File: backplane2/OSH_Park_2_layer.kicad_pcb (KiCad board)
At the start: 2 copper layers, 27 parts, among them J1 Conn_02x40_Odd_Even, J10 Conn_01x40, J11 Conn_01x40, J12 Conn_01x40, J13 Conn_01x40, J14 Conn_01x40, J15 Conn_01x40, J16 Conn_01x40, J17 Conn_01x40, J18 Conn_01x40, J19 Conn_01x40, J2 Conn_02x40_Odd_Even, J20 Conn_01x02, J21 OSTTA020161, J3 Conn_02x40_Odd_Even, J4 Conn_02x40_Odd_Even, J5 Conn_02x40_Odd_Even, J6 Conn_02x40_Odd_Even, J7 Conn_02x40_Odd_Even

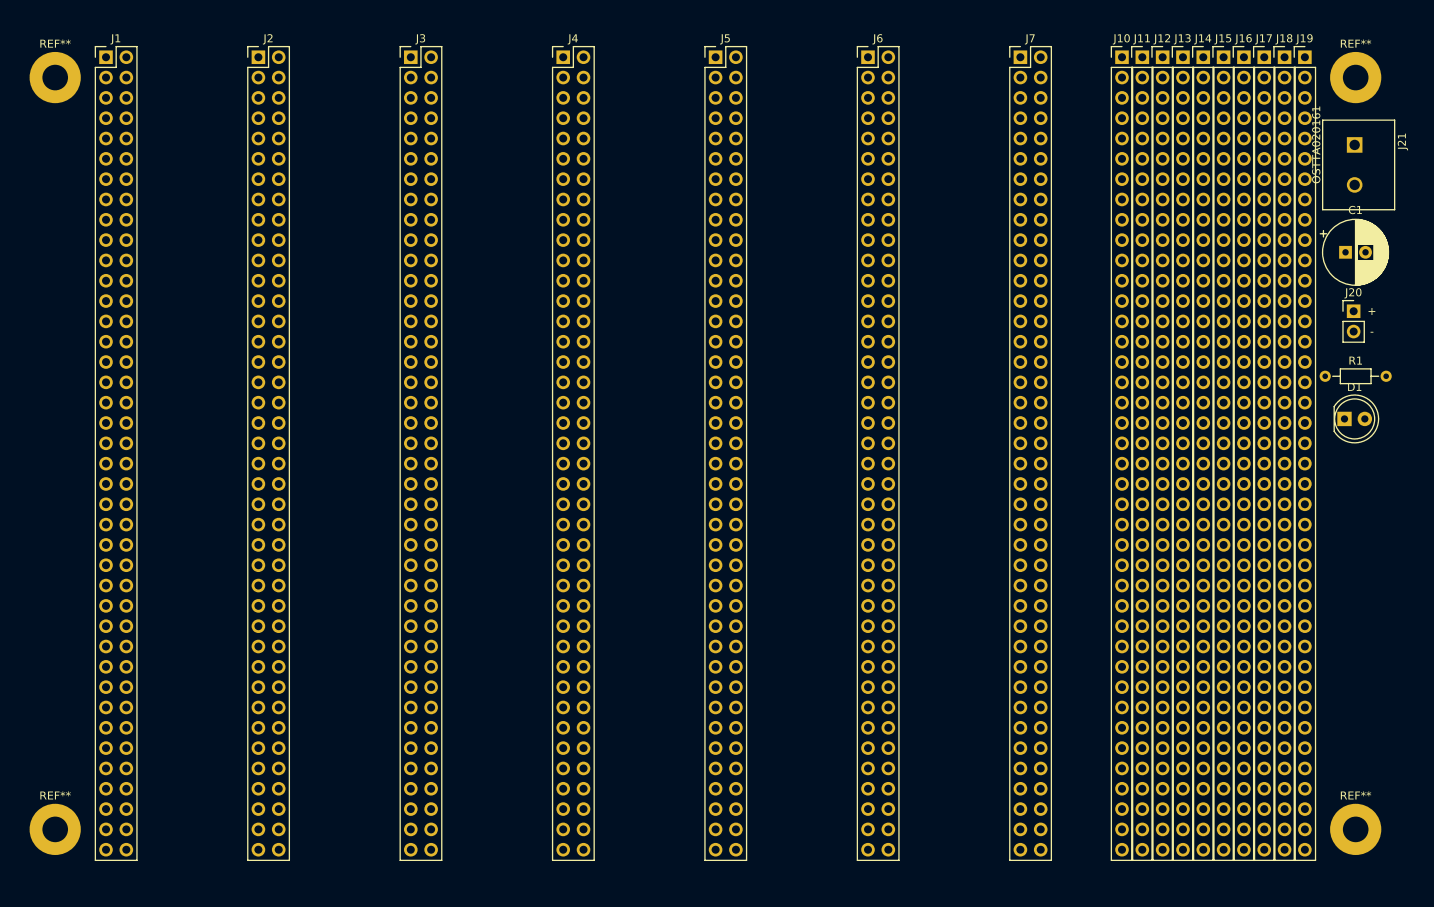
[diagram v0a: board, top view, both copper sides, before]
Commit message: routed half of the backplane connections
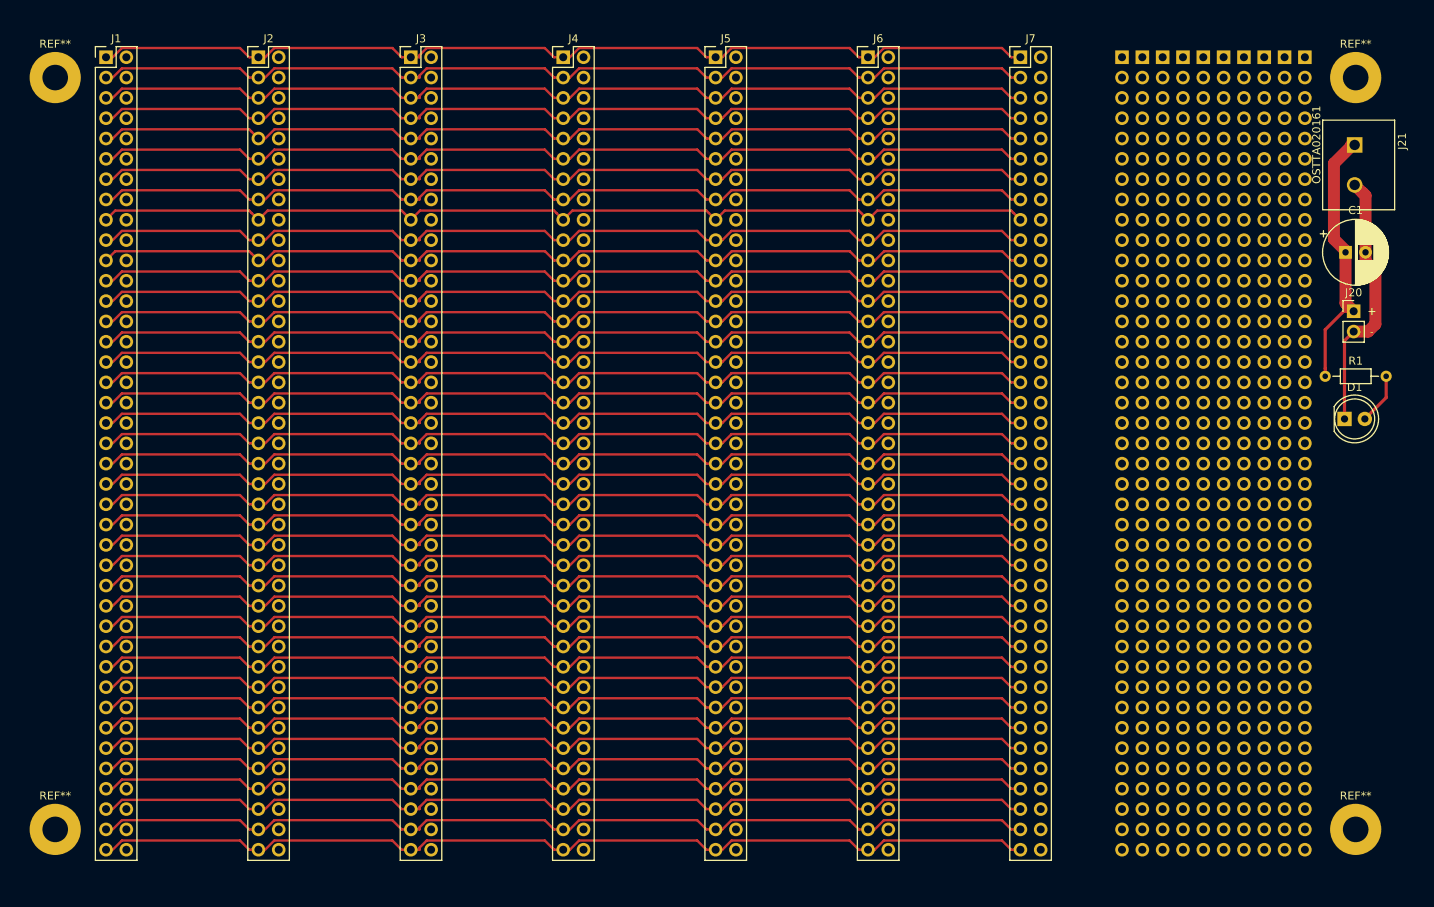
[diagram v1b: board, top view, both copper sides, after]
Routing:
- net /D1: track 0.00 -> 120.3 mm
- net /D17: track 0.00 -> 120.0 mm
- net /D9: track 0.00 -> 119.3 mm
- net /D21: track 0.00 -> 119.3 mm
- net /D79: track 0.00 -> 118.5 mm
- net /D65: track 0.00 -> 118.5 mm
- net /D49: track 0.00 -> 118.5 mm
- net /D45: track 0.00 -> 118.5 mm
- net /D31: track 0.00 -> 118.5 mm
- net /D13: track 0.00 -> 118.5 mm
- net /D7: track 0.00 -> 118.5 mm
- net /D5: track 0.00 -> 118.5 mm
- net /D3: track 0.00 -> 118.5 mm
- net /D11: track 0.00 -> 118.5 mm
- net /D77: track 0.00 -> 118.5 mm
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
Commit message: completely routed?
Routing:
- net /D80: track 0.00 -> 120.0 mm
- net /D66: track 0.00 -> 120.0 mm
- net /D50: track 0.00 -> 120.0 mm
- net /D46: track 0.00 -> 120.0 mm
- net /D32: track 0.00 -> 120.0 mm
- net /D14: track 0.00 -> 120.0 mm
- net /D8: track 0.00 -> 120.0 mm
- net /D6: track 0.00 -> 120.0 mm
- net /D4: track 0.00 -> 120.0 mm
- net /D10: track 0.00 -> 120.0 mm
- net /D36: track 0.00 -> 120.0 mm
- net /D18: track 0.00 -> 120.0 mm
- net /D2: track 0.00 -> 120.0 mm
- net /D78: track 0.00 -> 120.0 mm
- net /D76: track 0.00 -> 120.0 mm
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- added copper zone on B.Cu, net GND
- added copper zone on F.Cu, net VCC
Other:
- board outline added: 174.2 x 109.2 mm
- board text added: "generic passive backplane https://github.com/daveho/easycpu/backplane2 v0.1 30-Oct-2019"

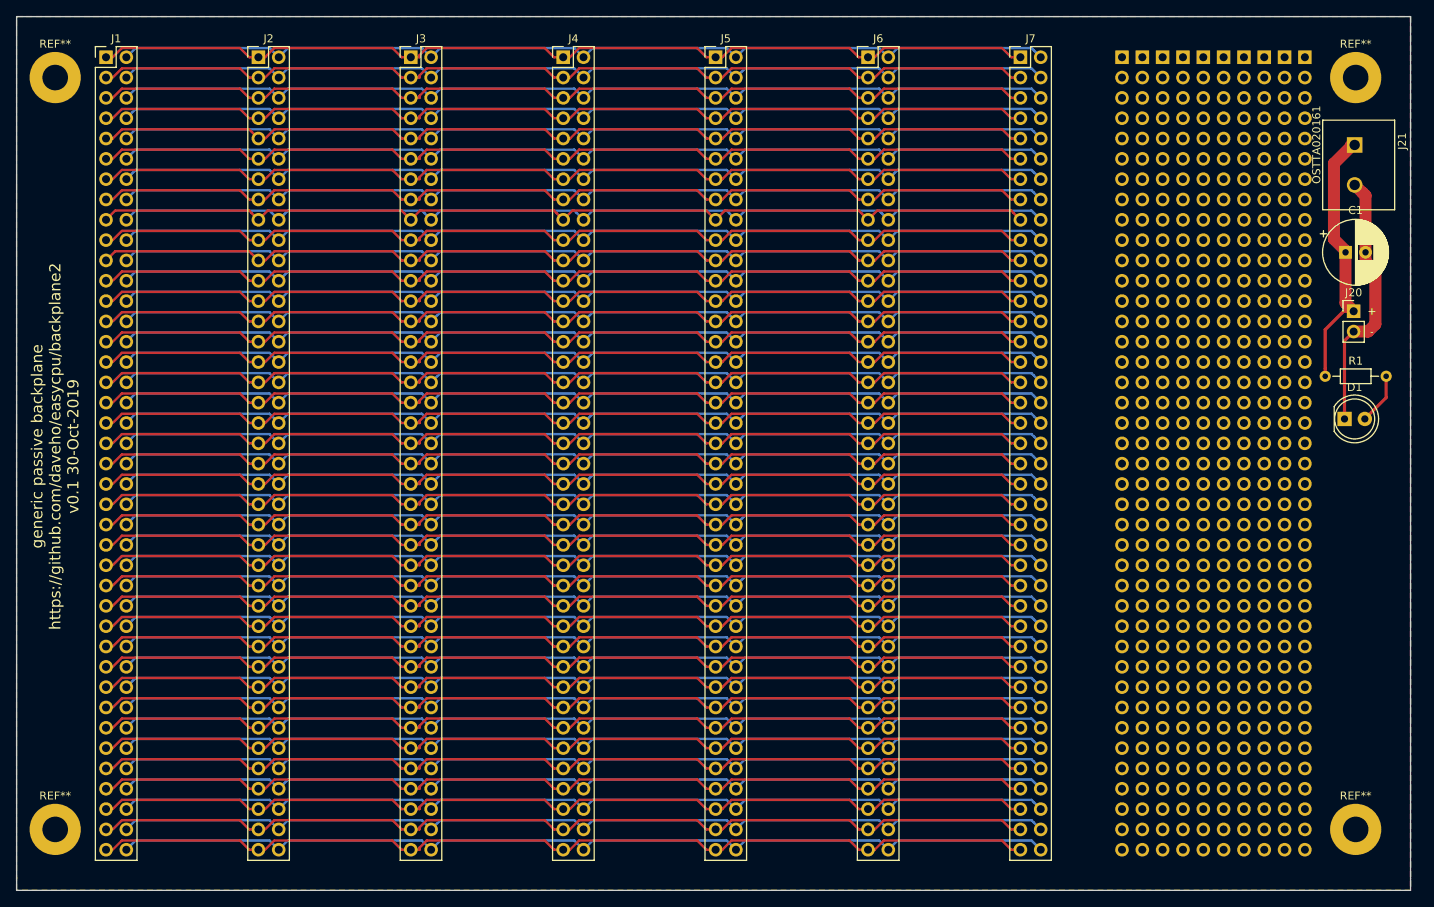
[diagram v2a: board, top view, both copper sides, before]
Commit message: added 4 power distribution traces
also fixed a couple of unconnected nets
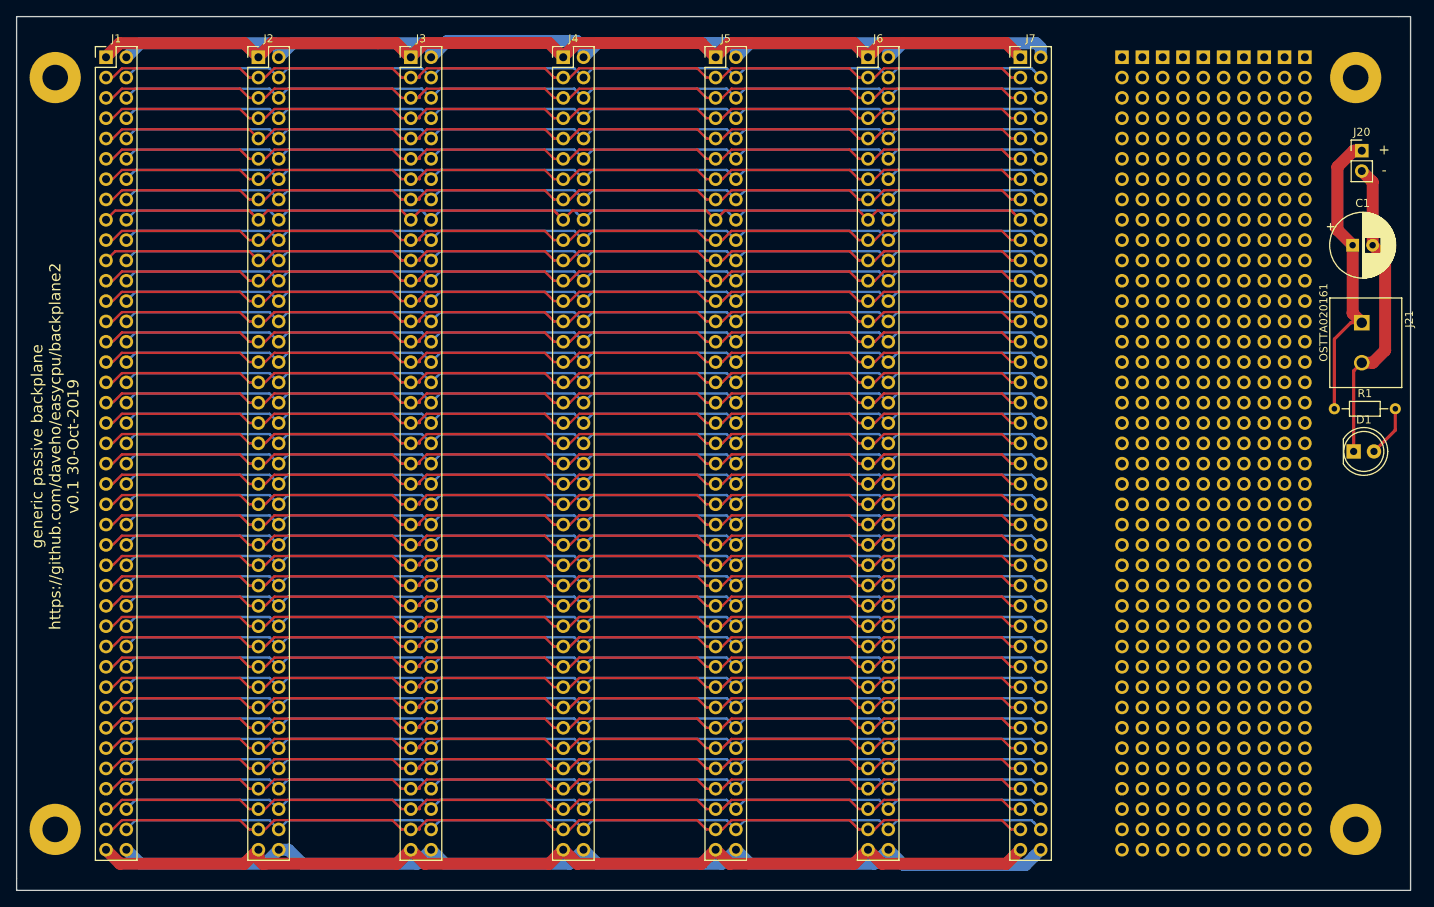
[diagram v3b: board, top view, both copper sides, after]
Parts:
- moved J21 22.2 mm to (207.8, 86.5)
- moved J20 20.1 mm to (207.8, 62.5)
- moved R1 4.22 mm to (204.3, 94.7)
- moved D1 4.22 mm to (206.8, 100.1)
- moved C1 1.26 mm to (206.6, 74.3)
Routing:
- net /D2: track 120.0 -> 127.5 mm
- net /D79: track 118.5 -> 124.5 mm
- net GND: track 33.0 -> 38.7 mm
- net /D1: track 120.3 -> 124.3 mm
- net /D80: track 120.0 -> 123.1 mm
- net VCC: track 34.5 -> 37.6 mm
- net /D21: track 119.3 -> 120.2 mm
- net /D9: track 119.3 -> 120.2 mm
- removed copper zone on B.Cu, net GND
- removed copper zone on F.Cu, net VCC

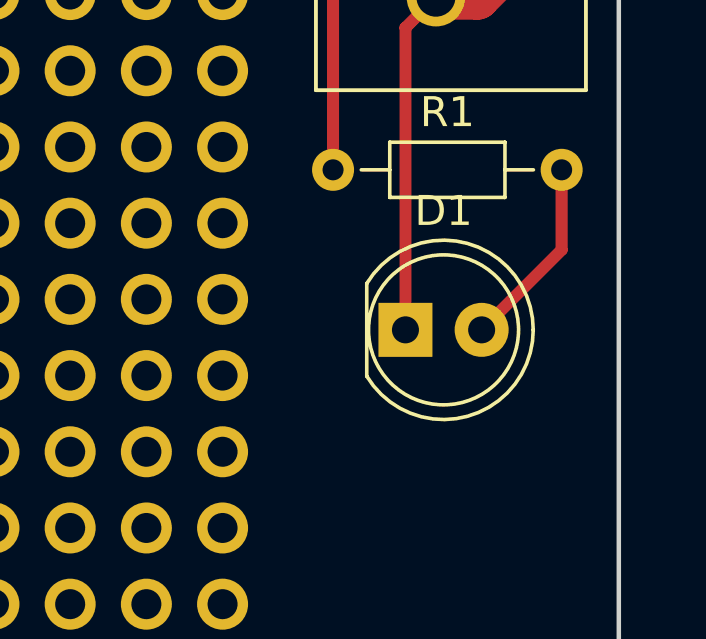
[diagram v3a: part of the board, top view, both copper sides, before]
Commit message: minor tweak to power LED placement
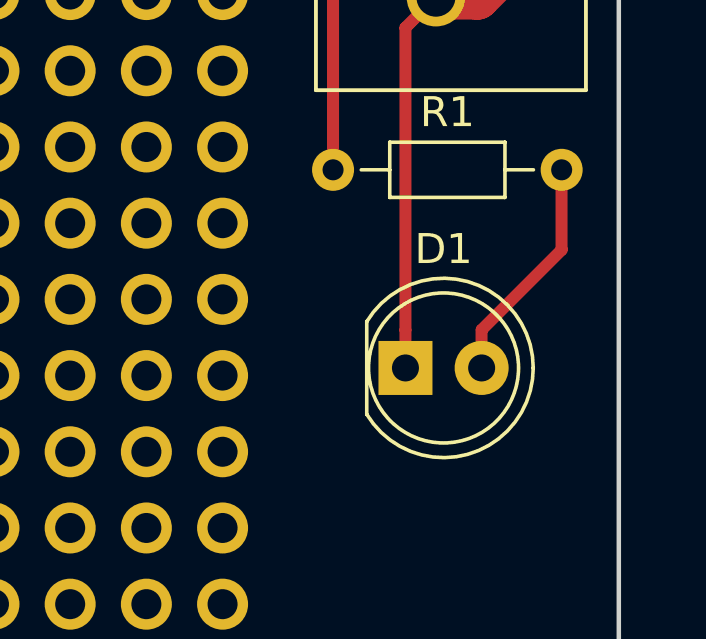
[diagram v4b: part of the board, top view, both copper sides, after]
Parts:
- moved D1 1.27 mm to (206.8, 101.3)
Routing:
- net Net-(D1-Pad2): track 6.44 -> 7.71 mm
- net GND: track 38.7 -> 40.0 mm
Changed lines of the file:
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@@
     (thickness 1.6)
     (drawings 10)
-    (tracks 2126)
+    (tracks 2128)
     (zones 0)
     (modules 27)
@@
   )
   (setup
-    (last_trace_width 0.3)
+    (last_trace_width 0.4)
     (user_trace_width 0.1524)
     (user_trace_width 0.2)
@@
   )
   (module LED_THT:LED_D5.0mm (layer F.Cu)
-    (at 206.756 100.076)
+    (at 206.756 101.346)
     (descr "LED, diameter 5.0mm, 2 pins, http://cdn-reichelt.de/documents/datenblatt/A500/LL-504BC2E-009.pdf")
     (tags "LED diameter 5.0mm 2 pins")
@@
   (segment (start 206.756 90.003) (end 207.772 88.987) (width 0.4) (layer F.Cu) (net 2))
   (segment (start 206.756 100.076) (end 206.756 90.003) (width 0.4) (layer F.Cu) (net 2))
+  (segment (start 206.756 100.076) (end 206.756 101.346) (width 0.4) (layer F.Cu) (net 2))
   (segment (start 211.963 97.409) (end 211.963 94.742) (width 0.4) (layer F.Cu) (net 3))
   (segment (start 209.296 100.076) (end 211.963 97.409) (width 0.4) (layer F.Cu) (net 3))
+  (segment (start 209.296 100.076) (end 209.296 101.346) (width 0.4) (layer F.Cu) (net 3))
   (segment (start 70.637599 151.612401) (end 72.39 149.86) (width 1.5) (layer B.Cu) (net 4))
   (segment (start 53.34 149.86) (end 55.092401 151.612401) (width 1.5) (layer B.Cu) (net 4))

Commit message: updated date (ready to fab now?)
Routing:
- added copper zone on B.Cu, net GND
- added copper zone on F.Cu, net VCC
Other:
- board text added: "generic passive backplane https://github.com/daveho/easycpu/backplane2 v0.1 31-Oct-2019"
- board text removed: "generic passive backplane https://github.com/daveho/easycpu/backplane2 v0.1 30-Oct-2019"
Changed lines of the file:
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@@
   (gr_line (start 212.344 45.72) (end 213.868 45.72) (layer Edge.Cuts) (width 0.15))
   (gr_line (start 39.624 45.72) (end 212.344 45.72) (layer Edge.Cuts) (width 0.15))
-  (gr_text "generic passive backplane\nhttps://github.com/daveho/easycpu/backplane2\nv0.1 30-Oct-2019" (at 44.45 99.441 90) (layer F.SilkS)
+  (gr_text "generic passive backplane\nhttps://github.com/daveho/easycpu/backplane2\nv0.1 31-Oct-2019" (at 44.45 99.441 90) (layer F.SilkS)
     (effects (font (size 1.4 1.4) (thickness 0.3)))
   )
@@
   (segment (start 147.774446 49.022) (end 163.322 49.022) (width 1.5) (layer F.Cu) (net 83))
   (segment (start 163.322 49.022) (end 165.1 50.8) (width 1.5) (layer F.Cu) (net 83))
+  (zone (net 1) (net_name VCC) (layer F.Cu) (hatch edge 0.508)
+    (connect_pads (clearance 0.508))
+    (min_thickness 0.254)
+    (fill yes (arc_segments 32) (thermal_gap 0.508) (thermal_bridge_width 0.508))
+    (polygon
+      (pts
+        (xy 39.624 45.72) (xy 213.868 45.72) (xy 213.868 154.94) (xy 39.624 154.94)
+      )
+    )
+  )
+  (zone (net 2) (net_name GND) (layer B.Cu) (hatch edge 0.508)
+    (connect_pads (clearance 0.508))
+    (min_thickness 0.254)
+    (fill yes (arc_segments 32) (thermal_gap 0.508) (thermal_bridge_width 0.508))
+    (polygon
+      (pts
+        (xy 39.624 45.72) (xy 213.868 45.72) (xy 213.868 154.94) (xy 39.624 154.94)
+      )
+    )
+  )
 )
